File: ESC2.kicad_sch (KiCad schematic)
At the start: 34 parts, among them J10 MOTOR2, J9 SWD2, Q5 XRS306D, Q6 XRS306D, Q7 XRS306D, U10 DRV8300D, U9 STM32G071GBUxN

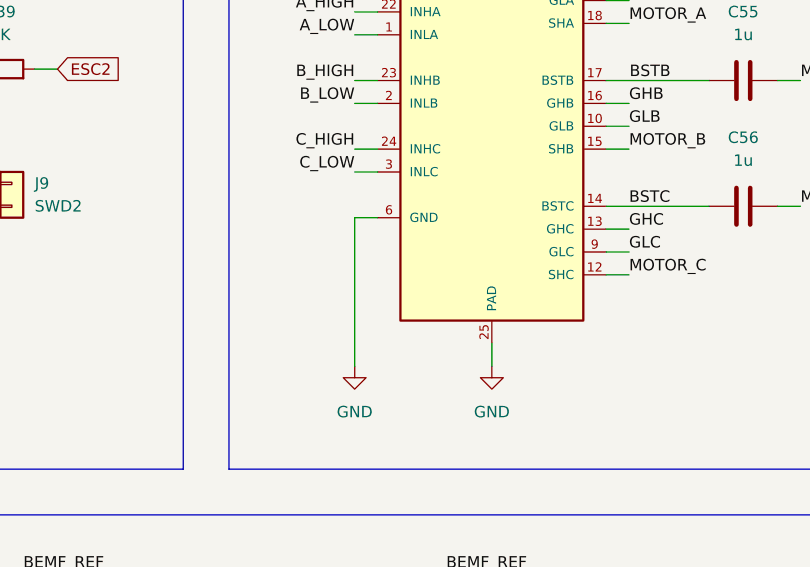
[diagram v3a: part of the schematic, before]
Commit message: Missing labels and revision
First complete revision of the schematic.
Added missing labels.

TODO:
Continue reviewing the schematic.
Include net coloring.
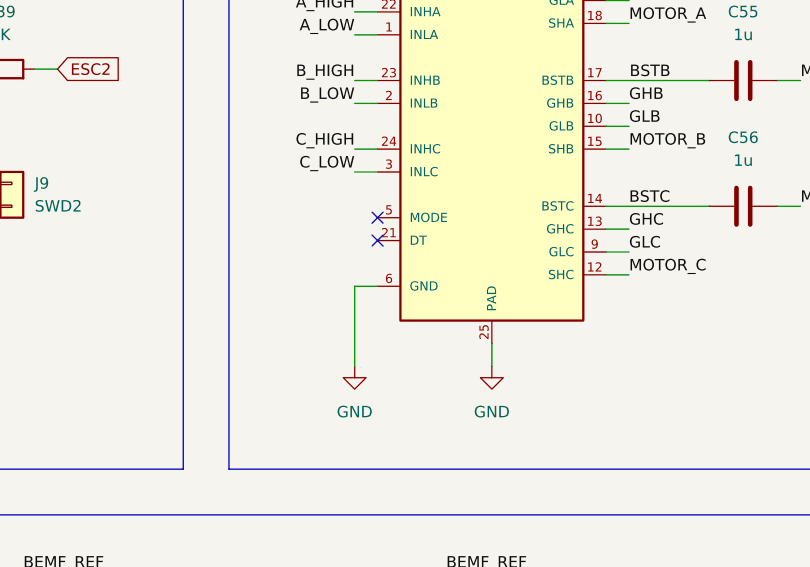
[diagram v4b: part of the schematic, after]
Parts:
- C47, C49, C50, C51, C52: footprint (none) -> Capacitor_SMD:C_1206_3216Metric
- J9: footprint (none) -> Custom_Parts:PAD_2_SQUARE_SOLID_1.0x1.0mm_P1.5mm
- Q5, Q6, Q7: footprint Custom_Parts:PDFN8 -> Custom_Parts:PDFN8_DUAL_3.3x3.3mm
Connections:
- no-connect marks 13 -> 15
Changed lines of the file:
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@@
 	)
 	(no_connect
+		(at 143.51 83.82)
+	)
+	(no_connect
 		(at 50.8 80.01)
 	)
@@
 		(at 50.8 72.39)
 	)
+	(no_connect
+		(at 143.51 81.28)
+	)
 	(wire
 		(pts
@@
 	(wire
 		(pts
+			(xy 140.97 88.9) (xy 140.97 97.79)
+		)
+		(stroke
+			(width 0)
+			(type default)
+		)
+	)
+	(wire
+		(pts
 			(xy 246.38 118.11) (xy 246.38 120.65)
 		)
@@
 	(wire
 		(pts
-			(xy 143.51 81.28) (xy 140.97 81.28)
-		)
-		(stroke
-			(width 0)
-			(type default)
-		)
-	)
-	(wire
-		(pts
 			(xy 231.14 39.37) (xy 238.76 39.37)
 		)
@@
 	(wire
 		(pts
-			(xy 151.13 133.35) (xy 153.67 133.35)
+			(xy 143.51 88.9) (xy 140.97 88.9)
 		)
 		(stroke
@@
 	(wire
 		(pts
-			(xy 140.97 81.28) (xy 140.97 97.79)
+			(xy 151.13 133.35) (xy 153.67 133.35)
 		)
 		(stroke
@@
 			)
 		)
-		(property "Footprint" "Custom_Parts:PDFN8"
+		(property "Footprint" "Custom_Parts:PDFN8_DUAL_3.3x3.3mm"
 			(at 248.92 95.25 0)
 			(effects
@@
 		(pin "4"
 		)
+		(pin "7"
+		)
+		(pin "8"
+		)
+		(pin "21"
+		)
+		(pin "5"
+		)
 		(instances
 			(project "ThunderHorse"
@@
 			)
 		)
-		(property "Footprint" "Custom_Parts:PDFN8"
+		(property "Footprint" "Custom_Parts:PDFN8_DUAL_3.3x3.3mm"
 			(at 248.92 82.55 0)
 			(effects
@@
 	(symbol
 		(lib_id "power:GND")
+		(at 140.97 97.79 0)
+		(unit 1)
+		(exclude_from_sim no)
+		(in_bom yes)
+		(on_board yes)
+		(dnp no)
+		(fields_autoplaced yes)
+		(property "Reference" "#PWR097"
+			(at 140.97 104.14 0)
+			(effects
+				(font
+					(size 1.27 1.27)
+				)
+				(hide yes)
+			)
+		)
+		(property "Value" "GND"
+			(at 140.97 102.87 0)
+			(effects
+				(font
+					(size 1.27 1.27)
+				)
+			)
+		)
+		(property "Footprint" ""
+			(at 140.97 97.79 0)
+			(effects
+				(font
+					(size 1.27 1.27)
+				)
+				(hide yes)
+			)
+		)
+		(property "Datasheet" ""
+			(at 140.97 97.79 0)
+			(effects
+				(font
+					(size 1.27 1.27)
+				)
+				(hide yes)
+			)
+		)
+		(property "Description" "Power symbol creates a global label with name \"GND\" , ground"
+			(at 140.97 97.79 0)
+			(effects
+				(font
+					(size 1.27 1.27)
+				)
+				(hide yes)
+			)
+		)
+		(pin "1"
+		)
+		(instances
+			(project "ThunderHorse"
+				(path "/ac187c6c-fa53-41cc-bce1-6f39a42a92e8/807a5f6f-4255-4cf0-8d90-acd62bb18590/5c810e84-f116-497a-8ed3-5f68f4ce3b3e"
+					(reference "#PWR097")
+					(unit 1)
+				)
+			)
+		)
+	)
+	(symbol
+		(lib_id "power:GND")
 		(at 151.13 146.05 0)
 		(unit 1)
@@
 			)
 		)
-		(property "Footprint" ""
+		(property "Footprint" "Capacitor_SMD:C_1206_3216Metric"
 			(at 37.7952 180.34 0)
 			(effects
@@
 			)
 		)
-		(property "Footprint" ""
+		(property "Footprint" "Capacitor_SMD:C_1206_3216Metric"
 			(at 75.8952 180.34 0)
 			(effects
@@
 			)
 		)
-		(property "Footprint" "Custom_Parts:PDFN8"
+		(property "Footprint" "Custom_Parts:PDFN8_DUAL_3.3x3.3mm"
 			(at 248.92 125.73 0)
 			(effects
@@
 			)
 		)
-		(property "Footprint" "Custom_Parts:PDFN8"
+		(property "Footprint" "Custom_Parts:PDFN8_DUAL_3.3x3.3mm"
 			(at 248.92 138.43 0)
 			(effects
@@
 			)
 		)
-		(property "Footprint" ""
+		(property "Footprint" "Custom_Parts:PAD_2_SQUARE_SOLID_1.0x1.0mm_P1.5mm"
 			(at 102.87 77.47 0)
 			(effects
@@
 			)
 		)
-		(property "Footprint" ""
+		(property "Footprint" "Capacitor_SMD:C_1206_3216Metric"
 			(at 88.5952 180.34 0)
 			(effects
@@
 			)
 		)
-		(property "Footprint" ""
+		(property "Footprint" "Capacitor_SMD:C_1206_3216Metric"
 			(at 50.4952 180.34 0)
 			(effects
@@
 			)
 		)
-		(property "Footprint" "Custom_Parts:PDFN8"
+		(property "Footprint" "Custom_Parts:PDFN8_DUAL_3.3x3.3mm"
 			(at 248.92 52.07 0)
 			(effects
@@
 	)
 	(symbol
-		(lib_id "power:GND")
-		(at 140.97 97.79 0)
-		(unit 1)
-		(exclude_from_sim no)
-		(in_bom yes)
-		(on_board yes)
-		(dnp no)
-		(fields_autoplaced yes)
-		(property "Reference" "#PWR097"
-			(at 140.97 104.14 0)
-			(effects
-				(font
-					(size 1.27 1.27)
-				)
-				(hide yes)
-			)
-		)
-		(property "Value" "GND"
-			(at 140.97 102.87 0)
-			(effects
-				(font
-					(size 1.27 1.27)
-				)
-			)
-		)
-		(property "Footprint" ""
-			(at 140.97 97.79 0)
-			(effects
-				(font
-					(size 1.27 1.27)
-				)
-				(hide yes)
-			)
-		)
-		(property "Datasheet" ""
-			(at 140.97 97.79 0)
-			(effects
-				(font
-					(size 1.27 1.27)
-				)
-				(hide yes)
-			)
-		)
-		(property "Description" "Power symbol creates a global label with name \"GND\" , ground"
-			(at 140.97 97.79 0)
-			(effects
-				(font
-					(size 1.27 1.27)
-				)
-				(hide yes)
-			)
-		)
-		(pin "1"
-		)
-		(instances
-			(project "ThunderHorse"
-				(path "/ac187c6c-fa53-41cc-bce1-6f39a42a92e8/807a5f6f-4255-4cf0-8d90-acd62bb18590/5c810e84-f116-497a-8ed3-5f68f4ce3b3e"
-					(reference "#PWR097")
-					(unit 1)
-				)
-			)
-		)
-	)
-	(symbol
 		(lib_id "Device:C")
 		(at 30.48 45.72 0)
@@
 			)
 		)
-		(property "Footprint" ""
+		(property "Footprint" "Capacitor_SMD:C_1206_3216Metric"
 			(at 63.1952 180.34 0)
 			(effects
@@
 			)
 		)
-		(property "Footprint" "Custom_Parts:PDFN8"
+		(property "Footprint" "Custom_Parts:PDFN8_DUAL_3.3x3.3mm"
 			(at 248.92 39.37 0)
 			(effects

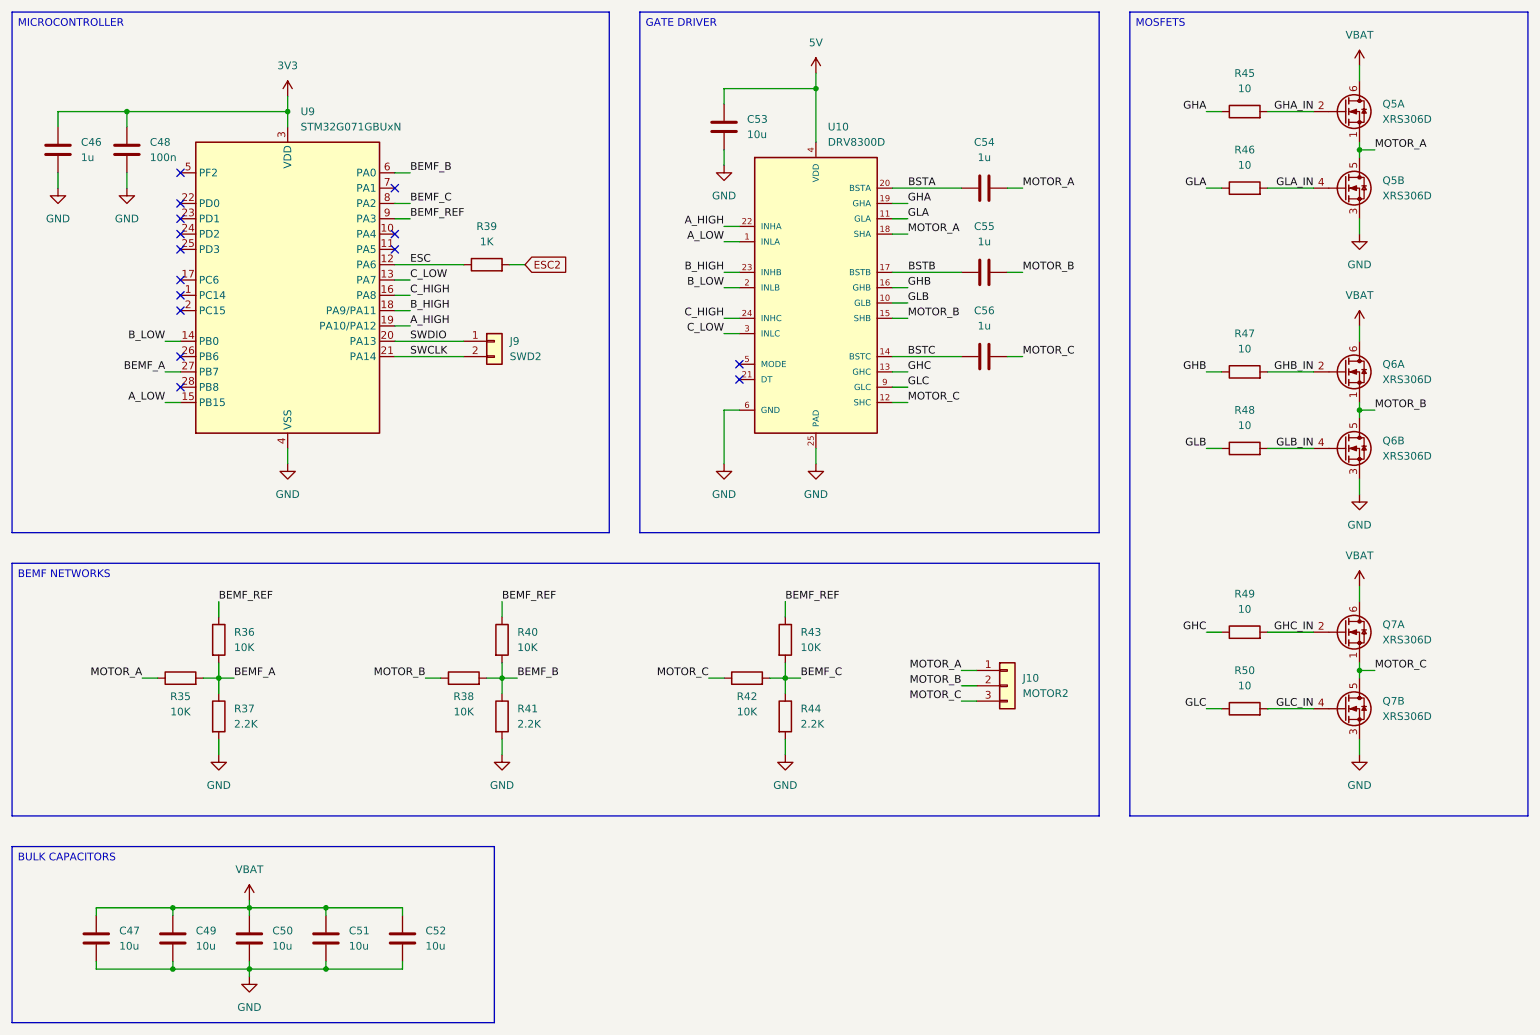
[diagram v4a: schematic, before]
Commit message: ESC layout and footprints
Added the initial ESC layout.
Updated some footprints for compatibility.
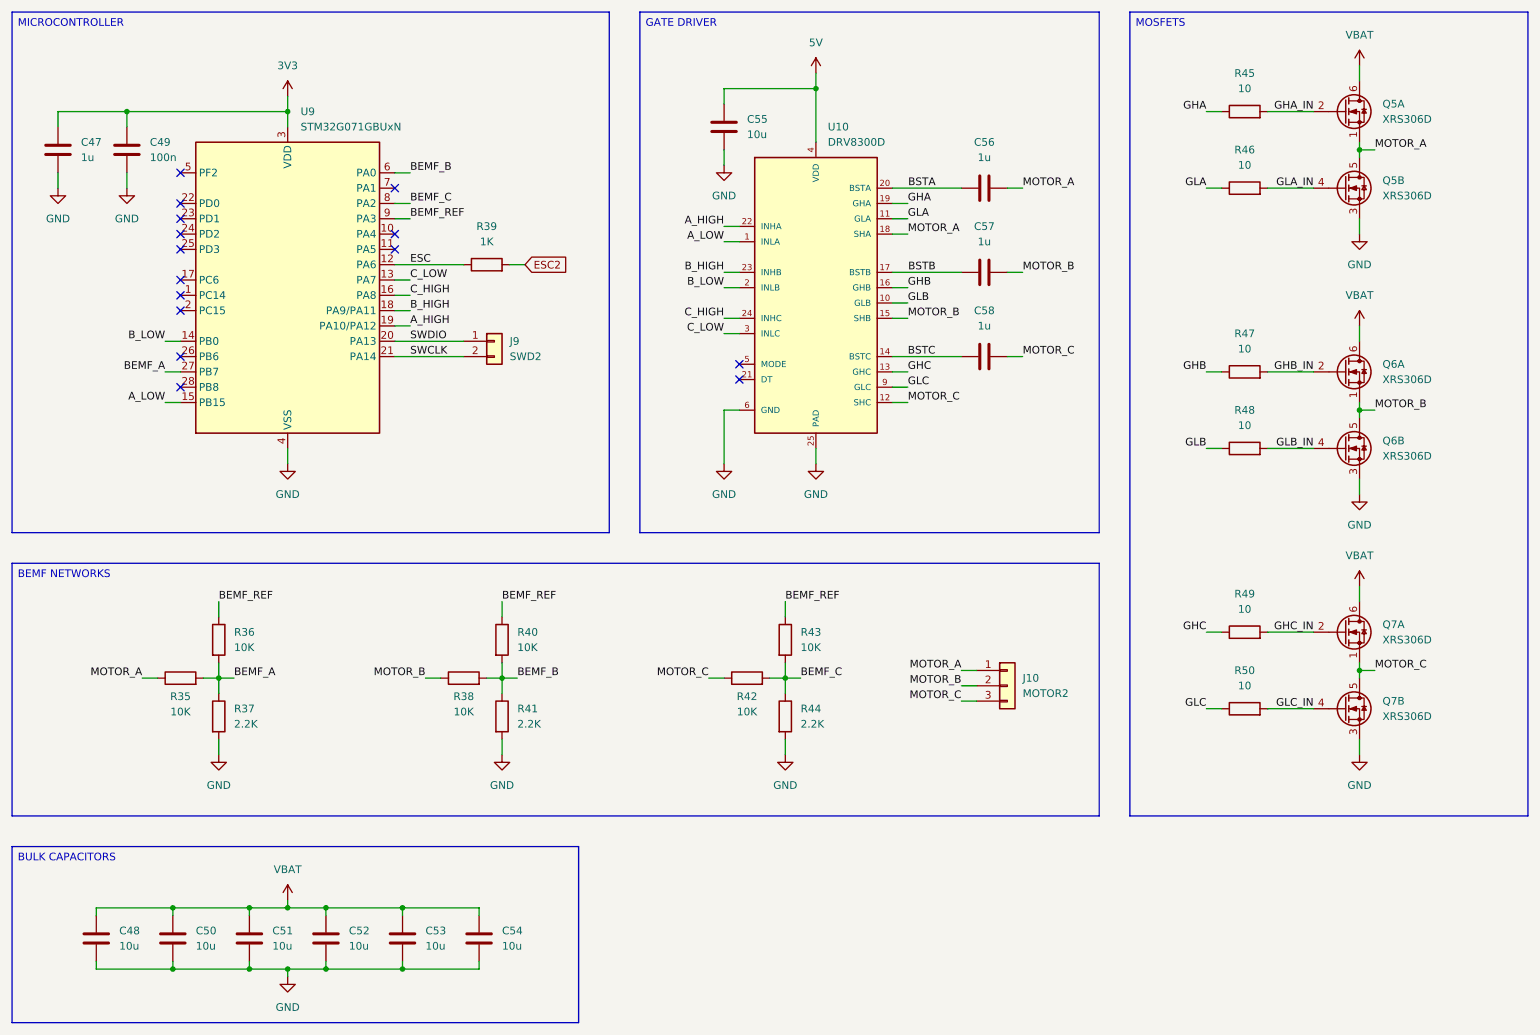
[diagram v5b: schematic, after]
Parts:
- removed C47, C49: 10u, Capacitor_SMD:C_1206_3216Metric, symbol Device:C
- added C48, C53, C54: 10u, Capacitor_SMD:C_1206_3216Metric, symbol Device:C
- J10: footprint Custom_Parts:PAD_3_SQUARE_SOLID_2.0x2.0mm_P2.5mm -> Custom_Parts:PAD_3_SQUARE_SOLID_2.5x2.5mm_P4.0mm
- renumbered C46 to C47, C48 to C49, C53 to C55, C54 to C56, C55 to C57, C56 to C58
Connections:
- net GND: now also C48.2, C53.2, C54.2
- net VBAT: now also C48.1, C53.1, C54.1

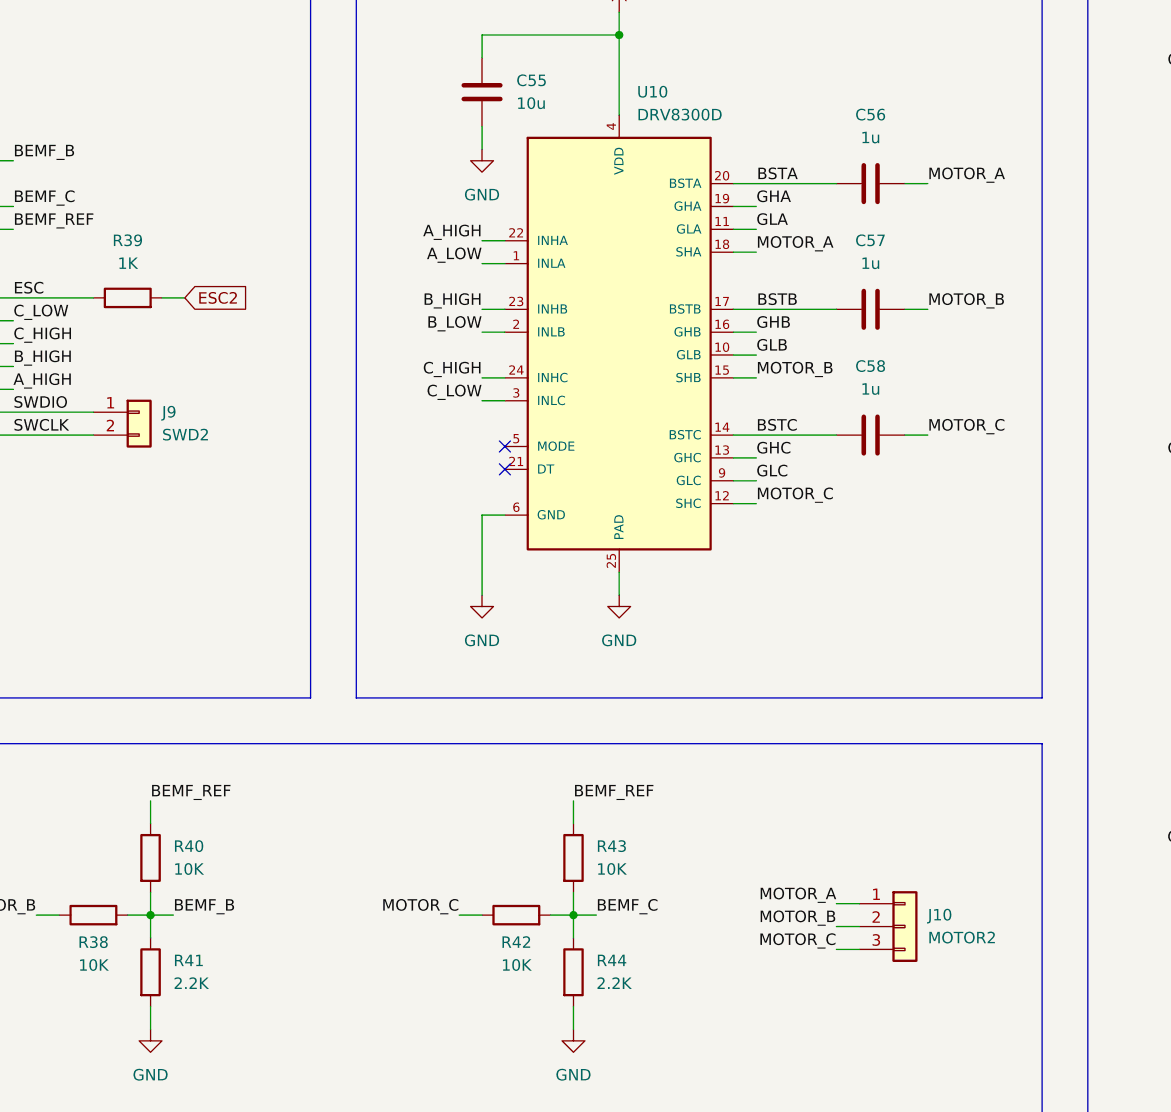
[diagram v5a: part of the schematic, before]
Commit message: Layout replication
Updated the ESC schematic to allow for layout replication.
Updated the PCB layout.
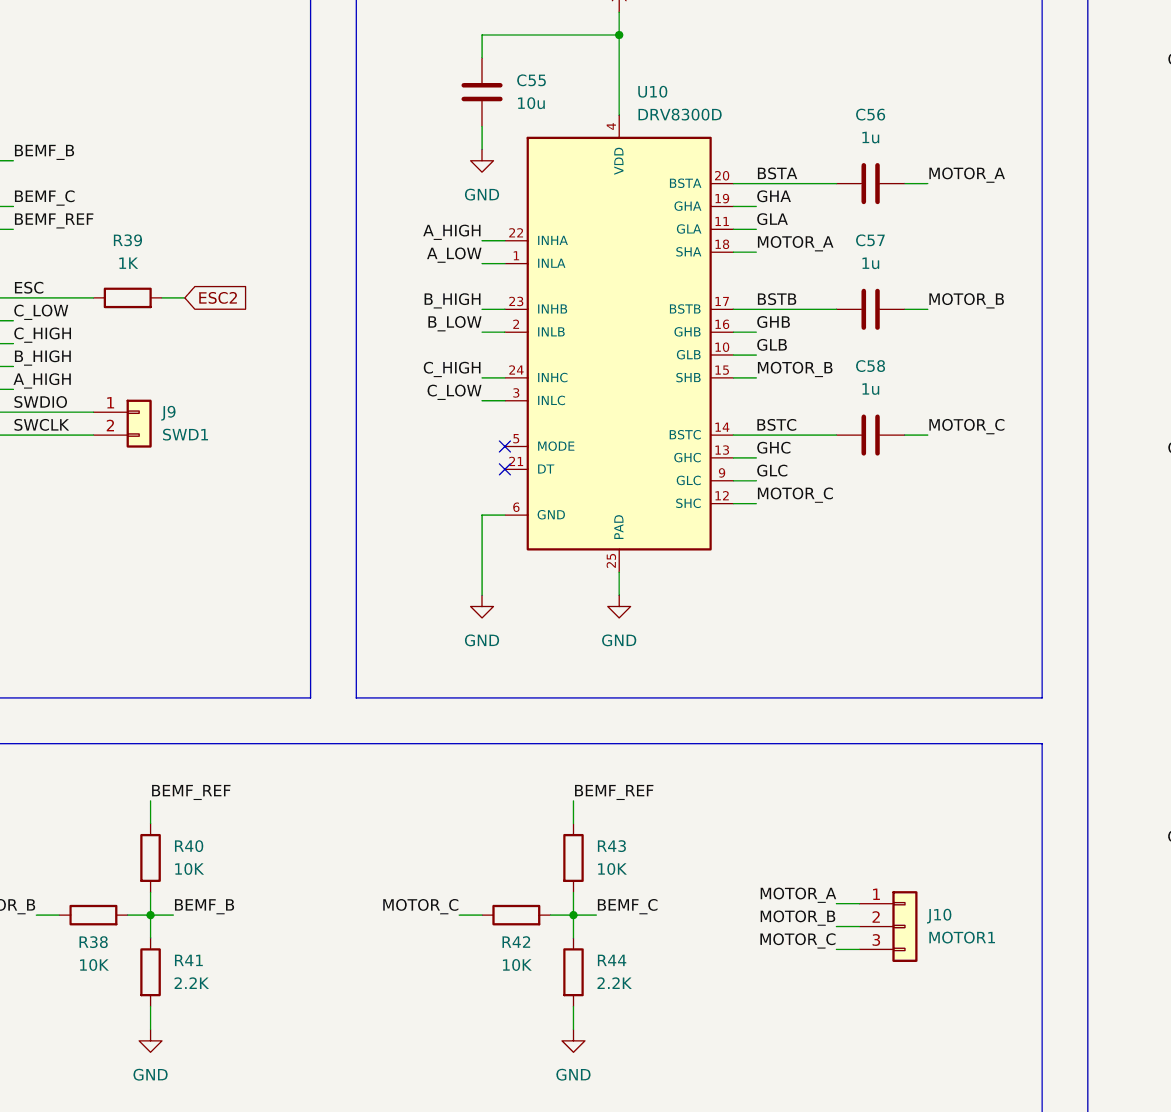
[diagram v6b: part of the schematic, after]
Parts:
- J10: value MOTOR2 -> MOTOR1
- J9: value SWD2 -> SWD1
